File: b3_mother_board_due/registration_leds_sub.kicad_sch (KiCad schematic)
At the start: 16 parts, among them J18 Upper A LED, J19 Upper B LED, J20 Lower A LED, J21 Lower B LED, Q1 BC547, Q2 BC547, Q3 BC547, Q4 BC547

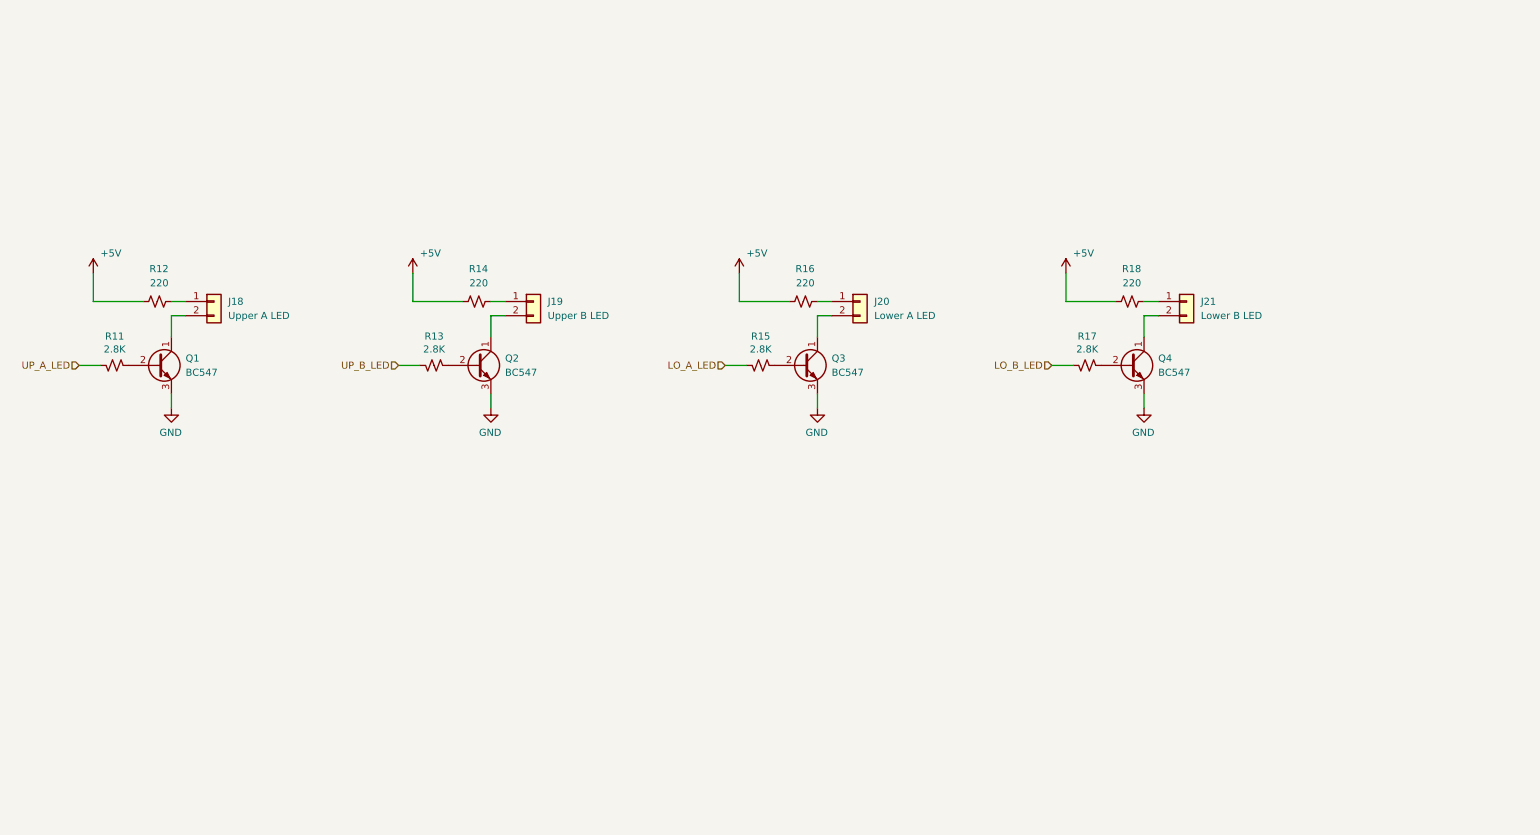
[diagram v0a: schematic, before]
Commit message: New organ architecture with mother board
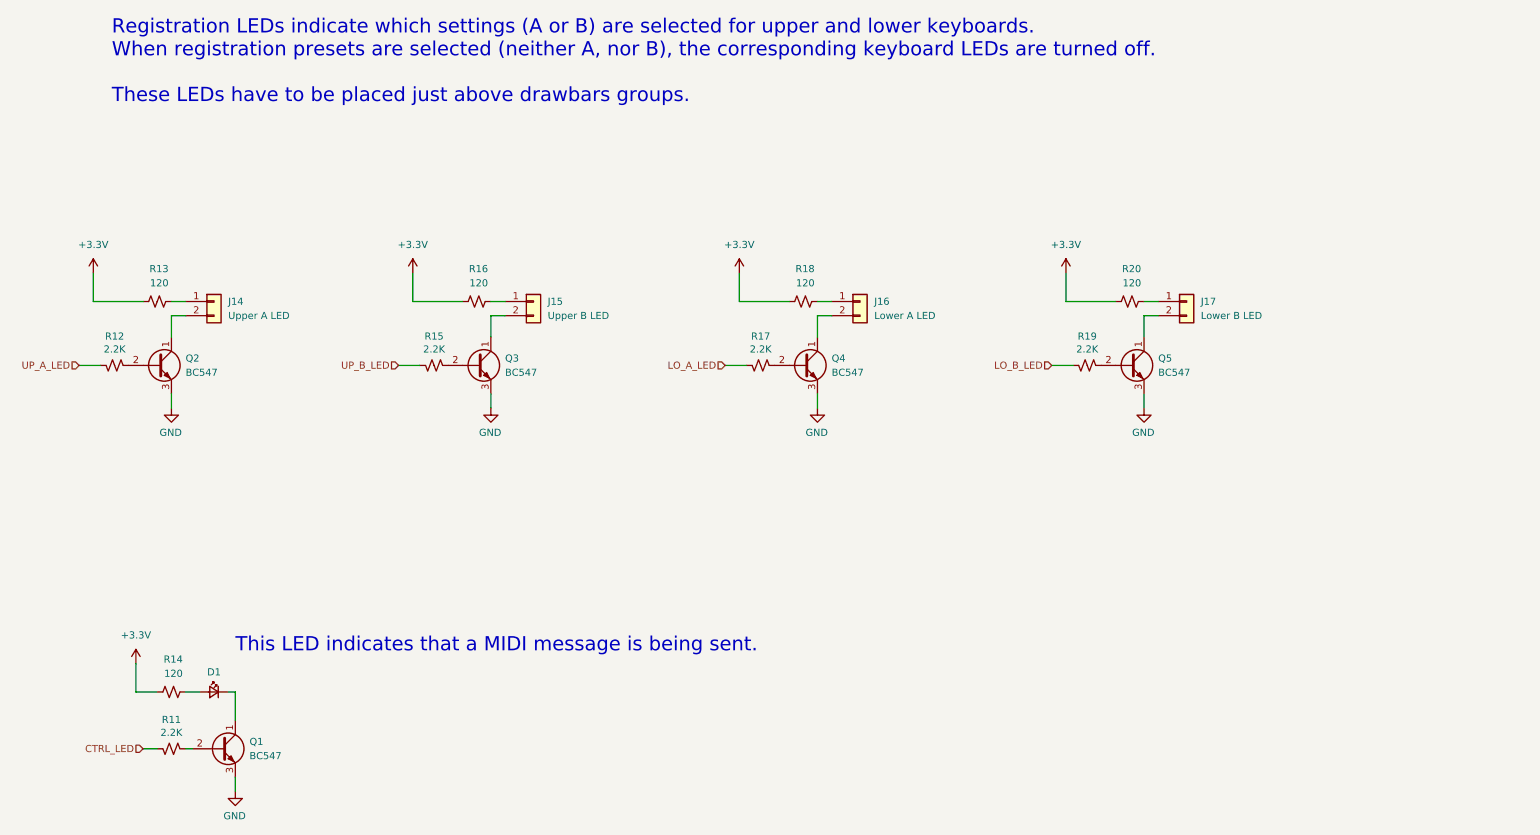
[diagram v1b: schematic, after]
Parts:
- added D1: Keyboards, LED_THT:LED_D3.0mm, symbol Device:LED_Small
- added Q1: BC547, Package_TO_SOT_THT:TO-92_Inline, symbol Transistor_BJT:BC547
- added R11: 2.2K, Resistor_THT:R_Axial_DIN0207_L6.3mm_D2.5mm_P7.62mm_Horizontal, symbol Device:R_Small_US
- added R14: 120, Resistor_THT:R_Axial_DIN0207_L6.3mm_D2.5mm_P7.62mm_Horizontal, symbol Device:R_Small_US
- R12: renamed from R11; value 2.8K -> 2.2K
- R13: renamed from R12; value 220 -> 120
- R15: renamed from R13; value 2.8K -> 2.2K
- R16: renamed from R14; value 220 -> 120
- R17: renamed from R15; value 2.8K -> 2.2K
- R18: renamed from R16; value 220 -> 120
- R19: renamed from R17; value 2.8K -> 2.2K
- R20: renamed from R18; value 220 -> 120
- renumbered J18 to J14, J19 to J15, J20 to J16, J21 to J17, Q1 to Q2, Q2 to Q3, Q3 to Q4, Q4 to Q5
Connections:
- net GND: now also Q1.3 (E)
- net +5V renamed +3.3V
- net +3.3V: now also R14.1
- new net: Q1.2 (B), R11.2
- new net: D1.1 (K), Q1.1 (C)
- new net: D1.2 (A), R14.2
- new net CTRL_LED: R11.1
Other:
- note added: "Registration LEDs indicate which settings (A or B) are selected for upper and lower keyboards. When registration presets are selected (neither A, nor B), the corresponding keyboard LEDs are turned off. These LEDs have to be placed just above drawbars groups."
- note added: "This LED indicates that a MIDI message is being sent."
